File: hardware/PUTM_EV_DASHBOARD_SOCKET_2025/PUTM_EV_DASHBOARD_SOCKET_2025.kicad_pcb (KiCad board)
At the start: 2 copper layers, 175.1 x 98.9 mm, 53 parts, among them J1 Conn_01x02_Pin, J1pin200000 Conn_02x20_Top_Bottom_Mountin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, J2 Conn_01x02_Pin, J2SO2 Conn_02x20_Top_Bottom_Mountin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, J3 Conn_01x02_Pin, J4 Conn_01x01, J5 Conn_01x01, J5POWER1 Conn_01x06_MountingPin, J7 FTSH, J8 Conn_01x03_Socket, Q4 BSS138, Q5 BSS138, Q6 BSS138, SW1 SW_Push, SW2 SW_Push, SW3 SW_Push, SW4 SW_Push, SW5 SW_Push, U1 SPX3819M5-L-5-0, U2 SPX3819M5-L-3-3

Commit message: 4
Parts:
- moved J8 50.5 mm to (246.9, 104.5)
- moved CS_BTN1 9.68 mm to (103.1, 53.6)
- moved RTD_BTN1 8.86 mm to (103.2, 69.2)
- moved SW4 6.95 mm to (94.0, 112.0), turned to 180 degrees
- moved TSA_BTN1 6.84 mm to (103.2, 83.6)
- moved R4 6.51 mm to (94.4, 112.2), turned to 180 degrees
- moved J1 6.42 mm to (96.3, 31.2)
- moved AMS0 6.42 mm to (96.2, 37.8)
- moved R9 6.42 mm to (96.2, 37.9)
- moved DRS_BTN1 6.26 mm to (103.2, 98.6)
- moved SW5 6.02 mm to (94.0, 97.0), turned to 180 degrees
- moved R5 5.86 mm to (94.2, 97.0), turned to 180 degrees
- moved SW3 5.43 mm to (94.0, 82.0), turned to 180 degrees
- moved R3 5.08 mm to (95.0, 81.4), turned to 180 degrees
- moved USR_BTN1 5.01 mm to (103.1, 113.7)
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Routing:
- net +3.3V: track 295.6 -> 359.4 mm
- net /SOCKETS_2X20/PH11: track 216.8 -> 230.1 mm
- net /SOCKETS_2X20/PB0: track 200.5 -> 187.8 mm
- net /SOCKETS_2X20/P14: track 187.3 -> 174.8 mm
- net /BUTTON_4: track 19.7 -> 28.2 mm
- net /SOCKETS_2X20/PA5: track 156.1 -> 162.7 mm
- net Net-(AMS0-K): track 76.7 -> 83.1 mm
- net /LED_1: track 79.7 -> 85.9 mm
- net /SOCKETS_2X20/PA15: track 176.7 -> 173.8 mm
- net /SOCKETS_2X20/PA3: track 214.7 -> 217.6 mm
- net /BUTTON_2: track 18.3 -> 20.2 mm
- net /SOCKETS_2X20/PH5: track 181.5 -> 183.4 mm
- net Net-(Q5-D): track 78.0 -> 79.1 mm
- net /BUTTON_3: track 19.8 -> 19.2 mm
- net /LED_3: track 81.6 -> 81.0 mm
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
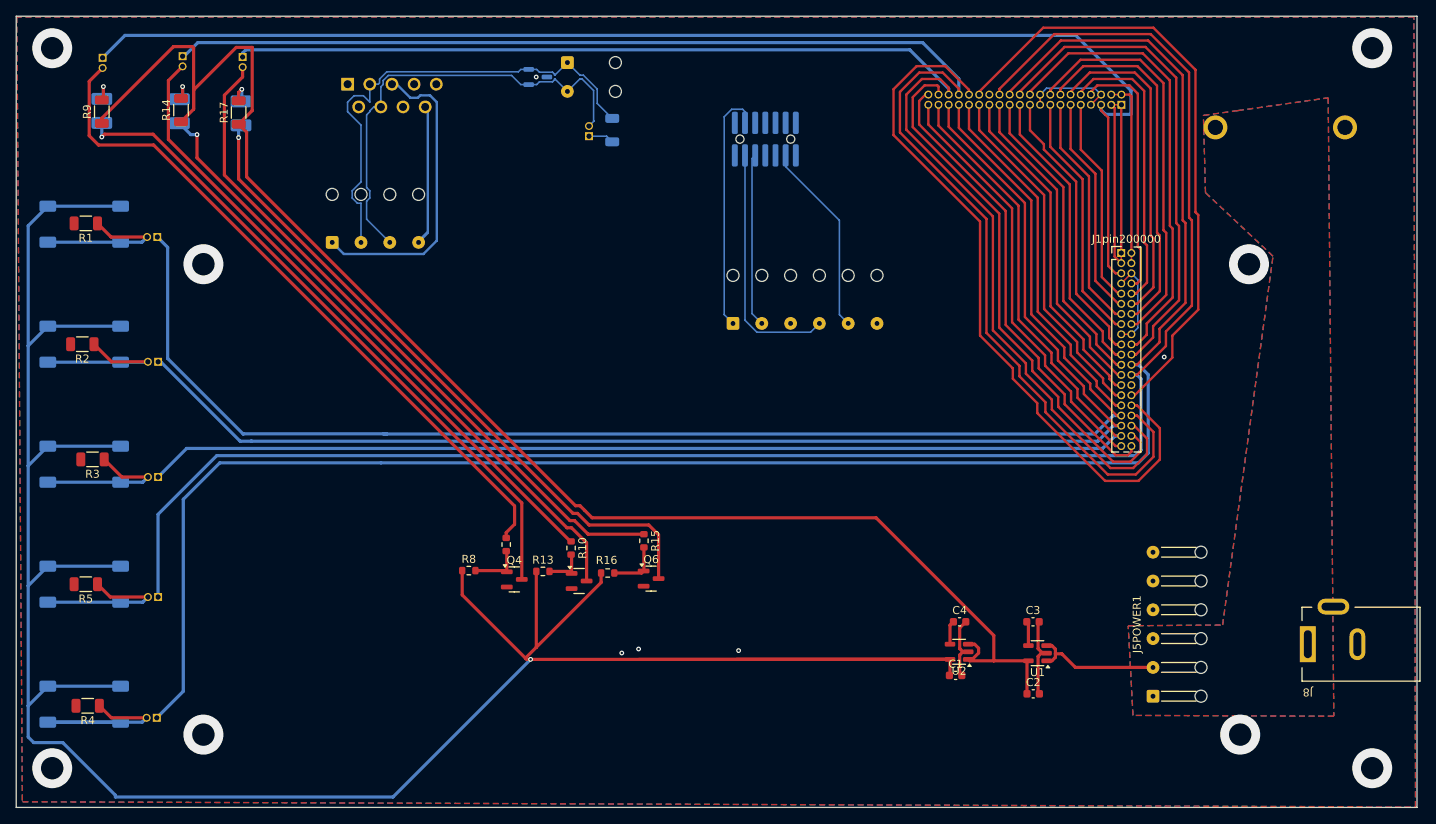
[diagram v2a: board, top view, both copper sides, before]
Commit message: poprawione opisy i złącze swd
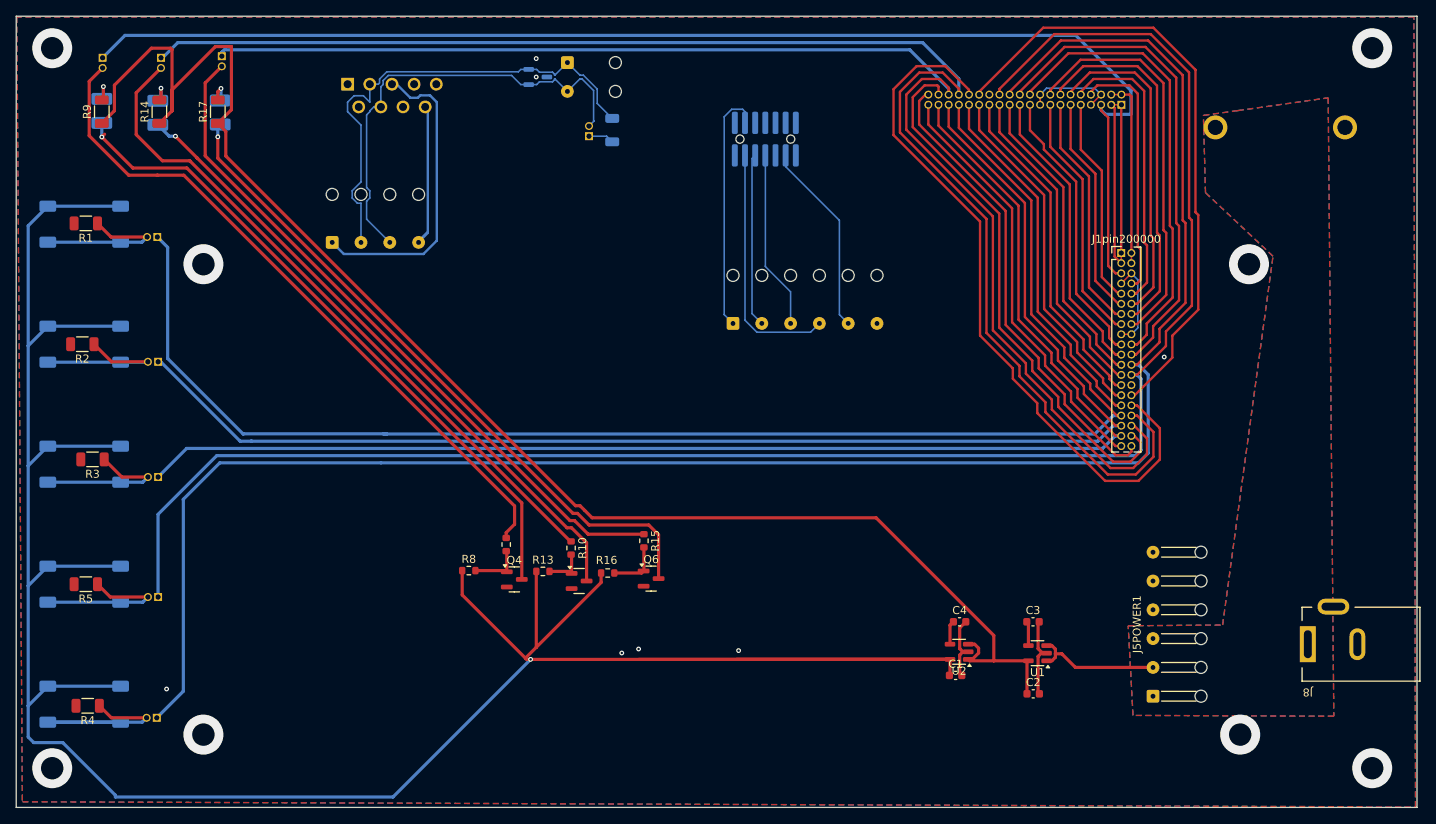
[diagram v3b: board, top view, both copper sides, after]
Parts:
- moved J2 2.71 mm to (103.6, 31.2)
- moved SAFETY_LED0 2.71 mm to (103.2, 38.1)
- moved R14 2.71 mm to (103.4, 37.9)
- moved FUSE_LED0 2.60 mm to (111.0, 38.0)
- moved J3 2.60 mm to (111.2, 31.0)
- moved R17 2.60 mm to (110.7, 37.9)
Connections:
- J7 pad 8: unconnected-(J7-Pin_8-Pad8) -> SWD_SWO
- SWD2 pad 3: GND -> SWD_SWO
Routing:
- net SWD_SWO: track 0.00 -> 22.3 mm
- net /LED_3: track 81.0 -> 85.0 mm
- net /SOCKETS_2X20/PH5: track 183.4 -> 186.2 mm
- net /SOCKETS_2X20/PH4: track 166.2 -> 168.8 mm
- net Net-(FUSE_LED0-K): track 83.6 -> 84.8 mm
- net /LED_2: track 85.5 -> 86.5 mm
- net Net-(Q5-D): track 79.1 -> 80.0 mm
- net GND: vias 13 -> 15
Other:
- board text added: "+"
- board text added: "-"
- board text added: "1_VCC_+5V 3_VCC_+5V 5_PA5 7_GND 9_PE40 11_P15 13_PB6 15_PB7 17_GND 19_PG3 21_PG4 23_PG2 25_PG9 27_PG10 29_PB10 31_PB5 33_PB0 35_P14 37_PA15 39_PA11"
- board text added: "2_VCC_+3.3V 4_VCC_+3.3V 6_GND 8_PA4 10_PB15 12_PB1 14_PC7 16_P10 18_GND 20_PA7 22_PA6 24_PH11 26_PA3 28_GND 30_PB2 32_PA8 34_PH5 36_PH4 38_PA10 40_PA12"
- board text added: "PA5-->AMS_LED PH5-->SAFETY_LED PH4-->FUSE_LED"
- board text added: "PB0-->CS_BTN1 P14-->RTD_BTN PA15-->TSA_BTN PA3-->DRS_BTN PH11-->URS_BTN"

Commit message: poprawione opisy i złącze swd, gnazdo POWER jest na krawędzi płytki
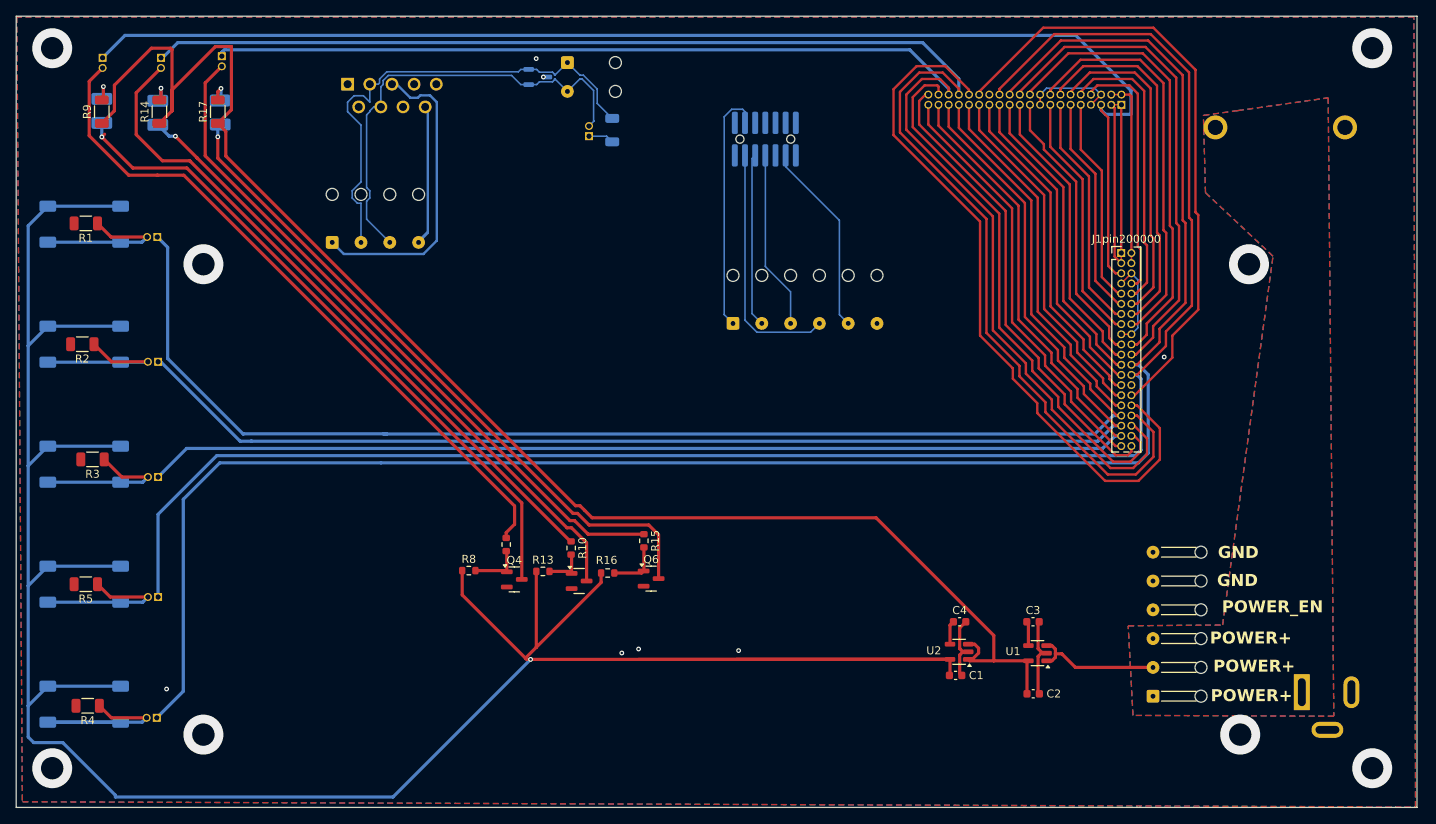
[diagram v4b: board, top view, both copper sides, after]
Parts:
- J8: moved to B.Cu
- moved J8 6.05 mm to (246.2, 110.5)
- renumbered AMS0 to AMS, CAN1 to CAN_1, CAN0 to CAN_2, CS_BTN1 to CS_BTN, DRS_BTN1 to DRS_BTN, FUSE_LED0 to FUSE_LED, J5POWER1 to POWER, RTD_BTN1 to RTD_BTN, SAFETY_LED0 to SAFETY_LED, TSA_BTN1 to TSA_BTN, USR_BTN1 to USR_BTN
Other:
- board text added: "GND"
- board text added: "POWER+"
- board text added: "POWER_EN"
- board text added: "RADOSŁAW BARYŁKO DASHBOARD_TESTBOARD v1.3"
- board text removed: "RADOSŁAW BARYŁKO DASHBOARD_TESTBOARD"

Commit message: gotowe
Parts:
- renumbered CAN_2 to CAN_1
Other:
- board text added: "RADOSŁAW BARYŁKO DASHBOARD_TESTBOARD v1.0"
- board text removed: "RADOSŁAW BARYŁKO DASHBOARD_TESTBOARD v1.3"
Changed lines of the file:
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@@
 		(descr "9-pin D-Sub connector, straight/vertical, THT-mount, socket (female), pitch 2.77x2.84mm, distance of mounting holes 25mm, see https://disti-assets.s3.amazonaws.com/tonar/files/datasheets/16730.pdf")
 		(tags "9-pin D-Sub connector straight vertical THT socket pitch 2.77x2.84mm mounting holes distance 25mm")
-		(property "Reference" "CAN_2"
+		(property "Reference" "CAN_1"
 			(at -5.37 6.4 0)
 			(layer "B.SilkS")
@@
 			(effects
 				(font
-					(size 1.5 1.5)
-					(thickness 0.3)
-					(bold yes)
+					(size 1 1)
+					(thickness 0.15)
 				)
 				(justify mirror)
@@
 		)
 	)
-	(gr_text "RADOSŁAW BARYŁKO\nDASHBOARD_TESTBOARD\nv1.3"
+	(gr_text "RADOSŁAW BARYŁKO\nDASHBOARD_TESTBOARD\nv1.0"
 		(at 191.9 98.7 0)
 		(layer "B.SilkS")

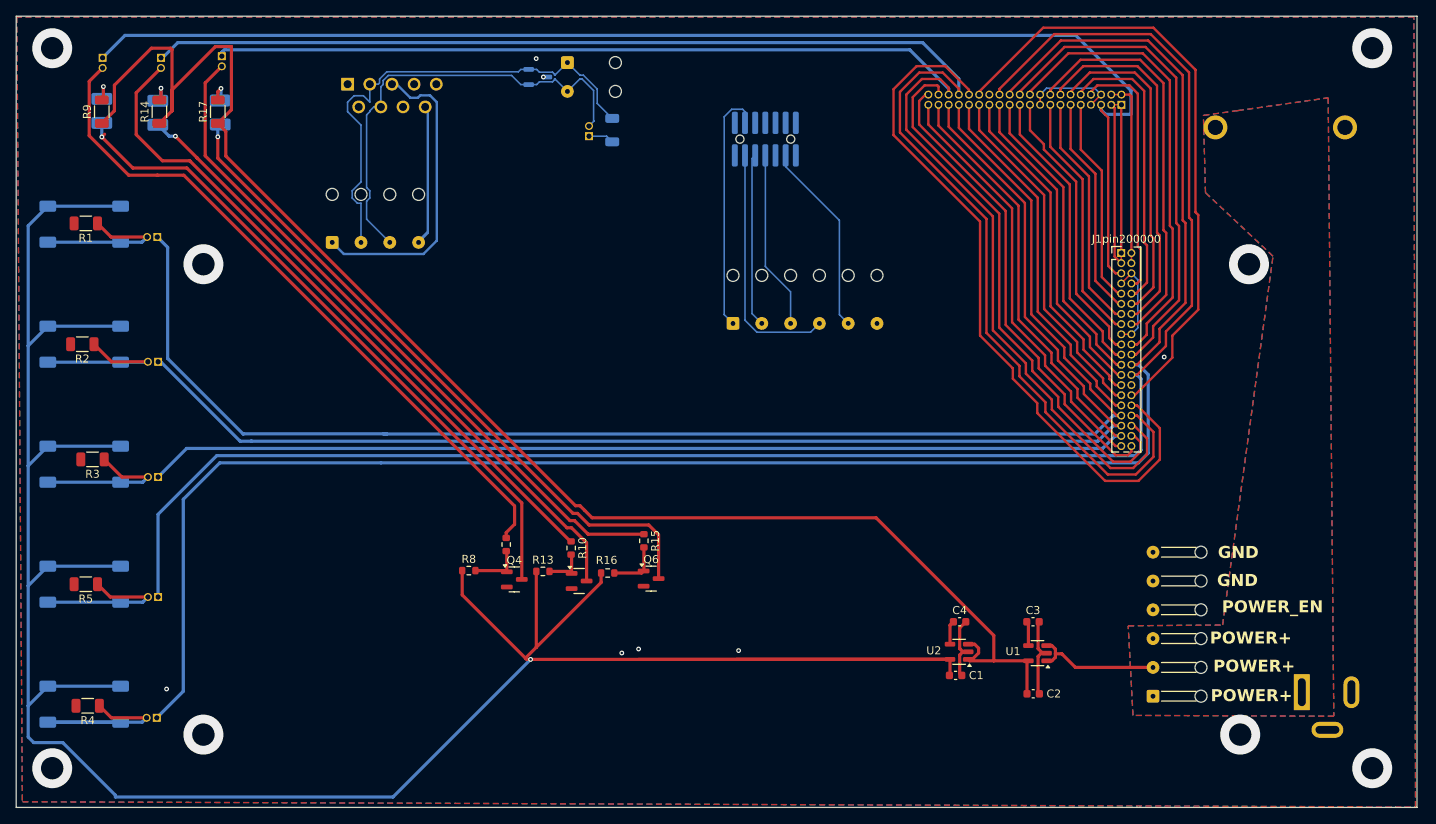
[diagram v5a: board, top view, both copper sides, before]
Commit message: dodano łezki do pól smd, pola lutownicze do przelotek, dodano zabezpieczenie przed odwrotna polaryzacją, odsunięto ścieżki od krawędzi płytki, poprawiono can,
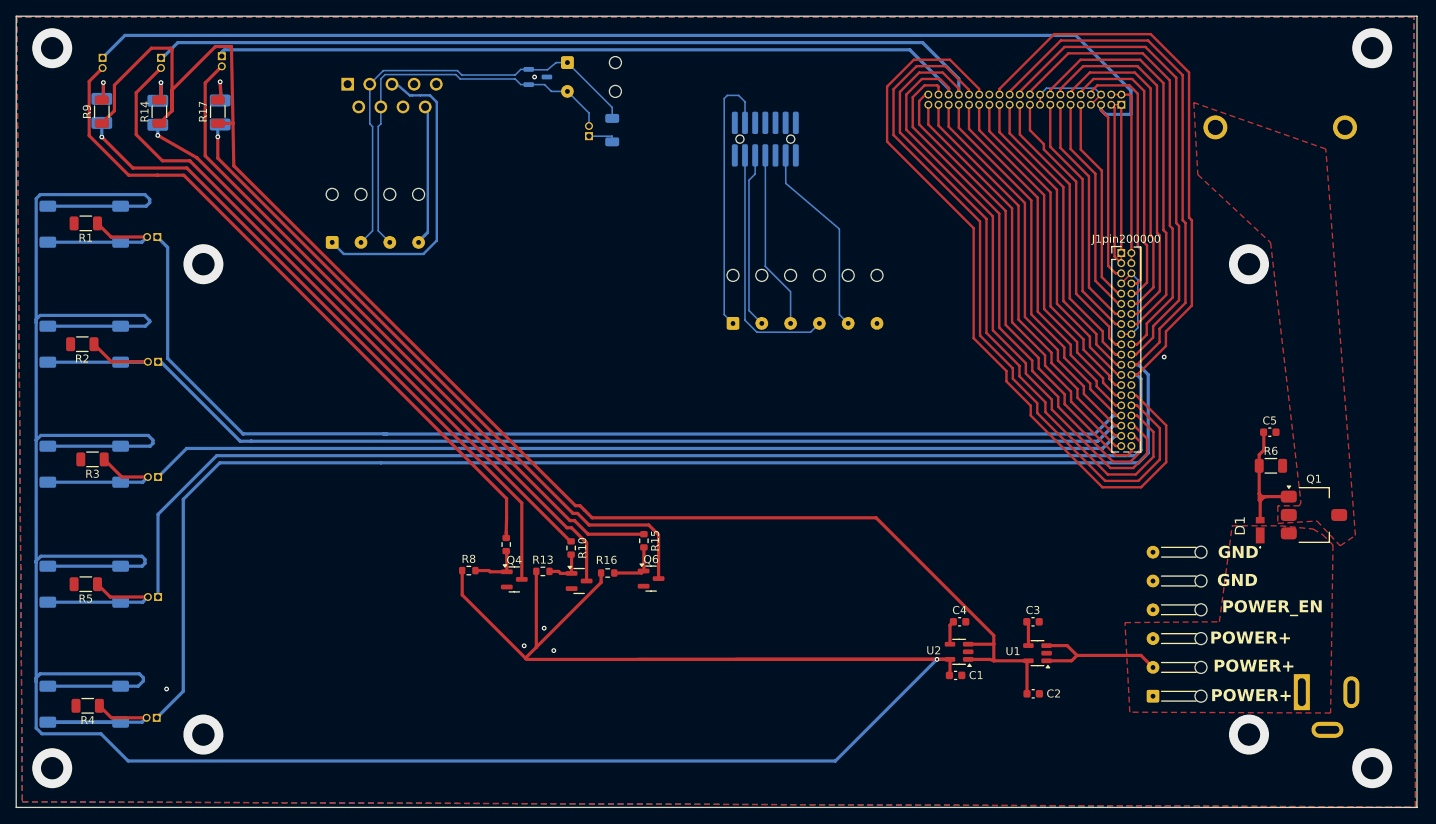
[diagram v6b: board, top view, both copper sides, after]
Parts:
- added C5: 22n, Capacitor_SMD:C_0603_1608Metric, F.Cu at (242.2, 78.0)
- added D1: TDZVTR12, SamacSys_Parts:TDZVTR20, F.Cu at (241.0, 90.2)
- added Q1: STN3P6F6, Package_TO_SOT_SMD:SOT-223-3_TabPin2, F.Cu at (247.7, 88.3)
- added R6: 150, Resistor_SMD:R_1206_3216Metric, F.Cu at (242.3, 82.2)
- renumbered AMS to AMS0, CAN_1 to CAN0, CAN_1 to CAN1, CS_BTN to CS_BTN1, DRS_BTN to DRS_BTN1, FUSE_LED to FUSE_LED0, POWER to J5POWER1, RTD_BTN to RTD_BTN1, SAFETY_LED to SAFETY_LED0, TSA_BTN to TSA_BTN1, USR_BTN to USR_BTN1
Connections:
- net SWD_SWO renamed /SWD/SWD_SWO
- J4 pad 1: /POWER/POWER1 -> /POWER/BANANA_JACK
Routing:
- net +3.3V: track 359.4 -> 484.2 mm
- net /SOCKETS_2X20/PB2: track 77.4 -> 96.1 mm
- net GND: track 41.6 -> 23.0 mm, vias 15 -> 14
- net Net-(D1-A): track 0.00 -> 16.3 mm
- net /CAN/CAN_P: track 57.2 -> 51.0 mm
- net /CAN/CAN_N: track 61.4 -> 56.1 mm
- net /SWD/SWD_VCC_+3.3V: track 30.8 -> 34.3 mm
- net /POWER/POWER1: track 16.5 -> 18.5 mm
- net Net-(FUSE_LED0-A): track 3.14 -> 4.99 mm
- net Net-(SAFETY_LED0-A): track 3.13 -> 4.53 mm
- net Net-(AMS0-A): track 3.38 -> 4.38 mm
- net /LED_1: track 85.9 -> 85.1 mm
- added copper zone on F.Cu, net /POWER/BANANA_JACK
- removed copper zone on B.Cu, net /POWER/POWER1

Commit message: Cosmetic corrections
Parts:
- added G***: LOGO, Logos:SignatureBox30mm, B.Cu at (182.5, 113.3)
- renumbered CAN0 to CAN1
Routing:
- net +3.3V: track 484.2 -> 353.2 mm
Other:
- board text added: "MICHAŁ BŁOTNIAK"
- board text removed: ".."

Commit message: Bogracz Czas przygotowania: 3 godziny 30 minut Liczba porcji: 2100 g gulaszu  W 100 g dania: Wartość energetyczna 156 kcal Węglowodany 5 g - W tym cukry 2 g Białko 7 g Tłuszcze 12 g
Składniki

800 g mięsa wołowego - np. pręga oraz łopatka
200 g boczku gotowanego wędzonego
100 g dobrej jakosci słoniny
6 łyżek dobrej jakości smalcu - około 100 g
2 średniej wielkości cebule - około 330 g
2 średniej wielkości czerwone papryki - około 400 g
5 ząbków czosnku - około 25 g
500 g ziemniaków - można pominąć lub dać kluseczki
2 łyżki koncentratu pomidorowego - do 50 g
400 ml wody - trochę więcej niż 1,5 szklanki
zioła i przyprawy: 2 listki laurowe, 3 ziarna ziela angielskiego; 1 pełna łyżeczka słodkiej papryki; 1 płaska łyżeczka soli; po pół łyżeczki wędzonej i ostrej papryki; 1/3 łyżeczki czarnego pieprzu
Składniki:
Bogracz
Szklanka ma u mnie pojemność 250 ml.

Warzywa ważone były przed ewentualnym obraniem/przygotowaniem. Zawsze podaję wagę użytych przeze mnie warzyw lub owoców. Nie trzeba jednak stosować się do wytycznych co do grama. Wagi podawane są po to, by łatwiej Wam było zorientować się, jaka mniej więcej ilość potrzebna jest do zrobienia danego dania.

Kalorie policzone zostały na podstawie użytych przeze mnie składników. Jest to więc orientacyjna liczba kalorii, ponieważ Twoje składniki mogą mieć inną liczbę kalorii niż te, których użyłam ja. Z podanej ilości składników otrzymasz Bogracz o wadze około 2100 gramów. Zanim zaczniesz szykować ten gulasz, polecam najpierw przeczytać cały przepis, by przygotować się odpowiednio wcześniej do kolejnych etapów wykonania.

UWAGA: Bogracz, to rodzaj kociołka stalowego lub emaliowanego, który rozszerza się ku górze. Kociołek podwieszany jest na trójnogu i wieszany na metalowym łańcuchu. Bogracz wisi nad ogniskiem, a w środku gotuje się węgierski gulasz. Zaczęto zatem nazywać tak samo i danie. Ponieważ zdecydowana większość Czytelników nie ma możliwości szykowania tego gulaszu w kociołku na świeżym powietrzu, podaję przepis na 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
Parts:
- renumbered CAN1 to CAN0
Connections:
- SWD2 pad 3: /SWD/SWD_SWO -> GND
- SWD2 pad 6: unconnected-(SWD2-Pin_6-Pad6) -> /SWD/SWD_SWO
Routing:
- net /SWD/SWD_SWO: track 22.3 -> 32.3 mm
